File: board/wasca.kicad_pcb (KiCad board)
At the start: 2 copper layers, 100.1 x 77.4 mm, 67 parts, among them CN1 CARTRIDGE_EDGE_CONNECTOR, CN2 TFP09-2-12B, CN3 Conn_02x02_Odd_Even, CN4 SODIMM-200, CN5 693063020911, U1 74ALVC164245, U10 SN74LVC1T45DBV, U11 SN74LVC1T45DBV, U12 SN74LVC1T45DBV, U13 ESP32_CAM_HALF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

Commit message: Cleanup
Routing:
- net /SDRAM_AUX_A2: track 24.3 -> 19.2 mm
- net /SDRAM_AUX_A1: track 20.6 -> 17.4 mm
- net /SDRAM_AUX_A10: track 17.7 -> 15.8 mm
- net /SDRAM_AUX_DQ5: track 26.4 -> 25.4 mm
- net GND: vias 175 -> 176

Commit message: Further cleanup
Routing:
- net /+3_3V: track 379.4 -> 378.7 mm
- net /SDRAM_AUX_DQ7: track 22.3 -> 23.0 mm
- net /SDRAM_AUX_A2: track 19.2 -> 18.7 mm
- net GND: vias 176 -> 180
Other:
- rule pad_to_mask_clearance: 0.05 -> 0

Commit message: Further cleanup
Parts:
- removed TP1, TP2: TestPoint, wasca:TEST_PAD
- added CN6: Conn_01x02_Pin, Connector_PinHeader_2.54mm:PinHeader_1x02_P2.54mm_Vertical, F.Cu at (30.3, 131.4)
- CHAMFER_WARN1, CHAMFER_WARN2: value LOGO -> CHAMFER_WARNING
- moved KICAD1 41.6 mm to (57.6, 96.3)
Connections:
- CN4 pad 150: Net-(CN4-Pad150) -> /TEST_2
- CN4 pad 89: Net-(CN4-Pad89) -> /TEST_1
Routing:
- net /TEST_1: track 0.00 -> 49.3 mm, vias 0 -> 1
- net /TEST_2: track 0.00 -> 30.1 mm, vias 0 -> 1
- net Net-(CN4-Pad150): track 12.0 -> 0.00 mm, vias 1 -> 0
- net Net-(CN4-Pad89): track 2.94 -> 0.00 mm, vias 1 -> 0
- net GND: vias 180 -> 181

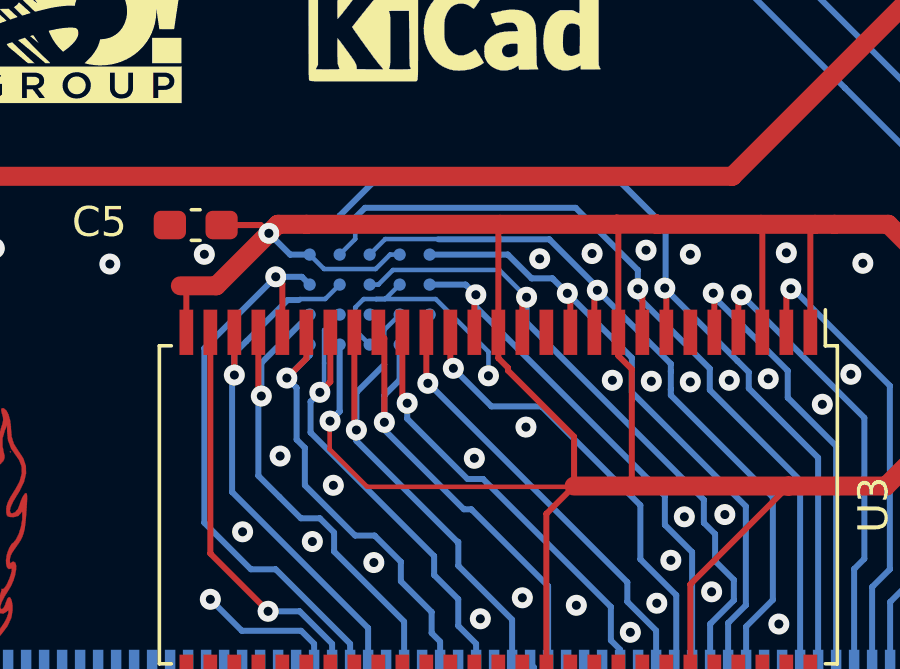
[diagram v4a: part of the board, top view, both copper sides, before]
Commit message: Remove HyperRAM
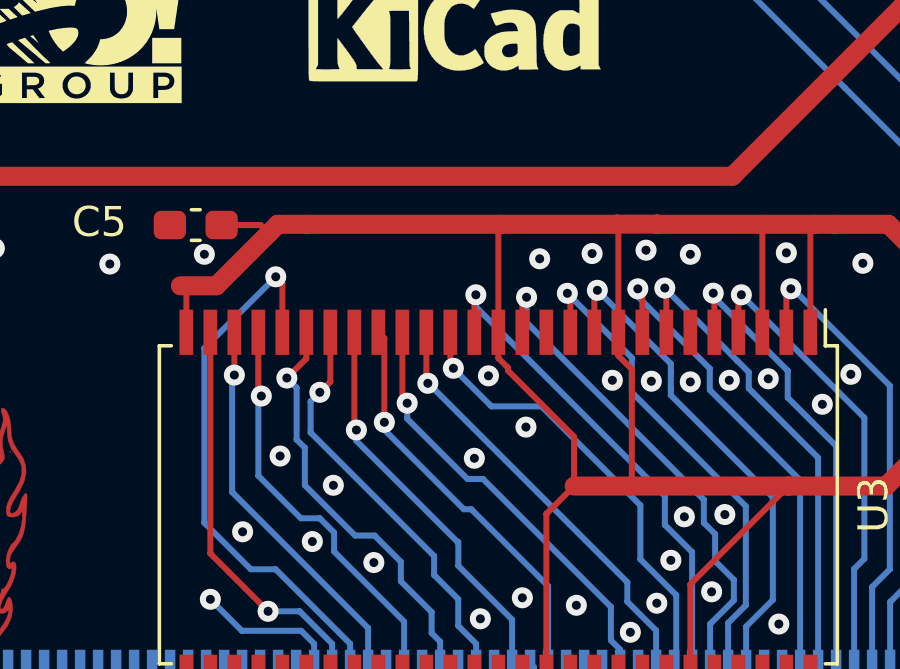
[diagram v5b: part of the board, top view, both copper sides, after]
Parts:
- removed U6: IS66WVH8M8ALL-166B1LI, wasca:BGA25C100P5X5_800X600X120N
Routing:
- net /+3_3V: track 378.7 -> 361.4 mm, vias 22 -> 20
- net /SDRAM_AUX_DQ3: track 30.9 -> 16.7 mm
- net /SDRAM_AUX_DQ4: track 29.8 -> 16.8 mm
- net /SDRAM_AUX_DQ5: track 25.8 -> 17.2 mm
- net GND: track 1221.9 -> 1213.4 mm
- net /SDRAM_AUX_DQ7: track 23.0 -> 17.2 mm
- net /SDRAM_AUX_A2: track 18.7 -> 13.5 mm
- net /SDRAM_AUX_DQ6: track 22.1 -> 16.9 mm
- net /SDRAM_AUX_BA0: track 18.2 -> 13.8 mm
- net /SDRAM_AUX_A1: track 17.4 -> 14.0 mm
- net /SDRAM_AUX_BA1: track 17.0 -> 14.1 mm
- net /SDRAM_AUX_CS: track 16.9 -> 14.1 mm
- net /SDRAM_AUX_DQM0: track 18.8 -> 17.1 mm
- net /SDRAM_AUX_A10: track 15.8 -> 14.3 mm
- net /SDRAM_AUX_A0: track 20.1 -> 18.9 mm

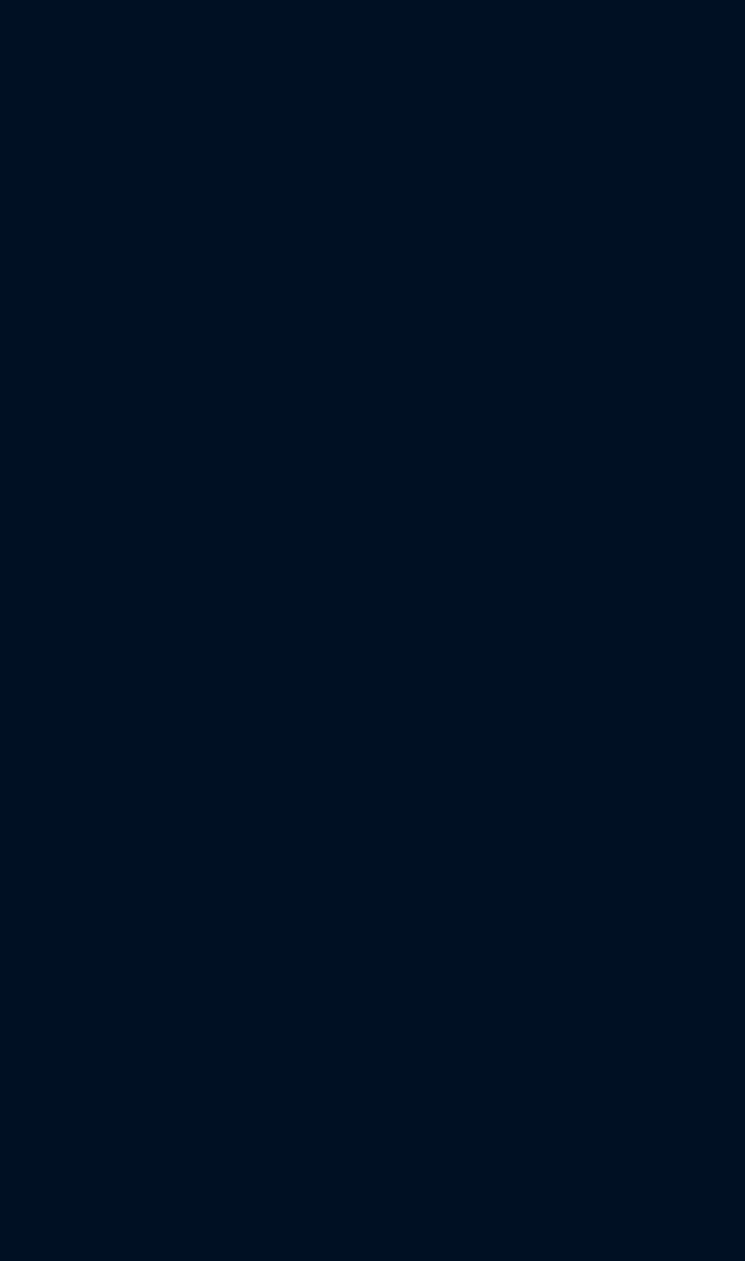
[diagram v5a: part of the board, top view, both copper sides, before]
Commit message: Adding FPGA+power supplies
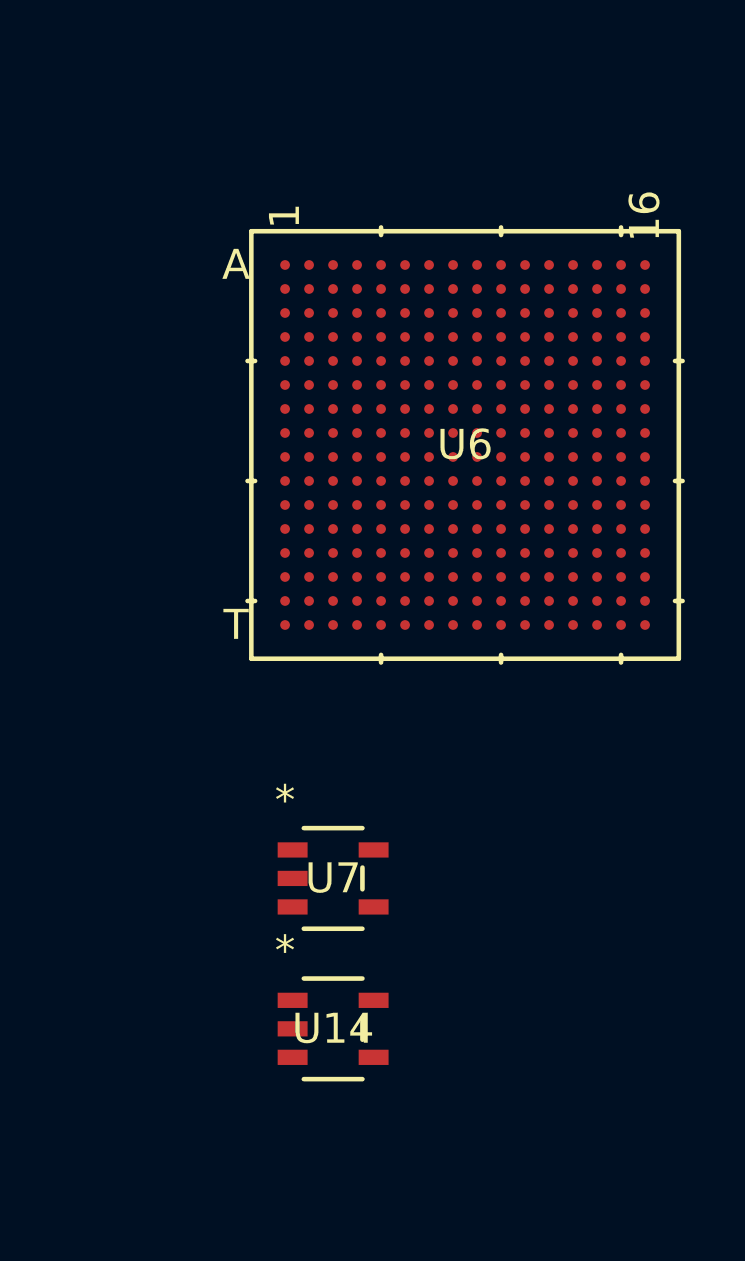
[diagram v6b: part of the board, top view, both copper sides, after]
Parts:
- added U14: SY8008CAAC, wasca:SOT23-5_SY8008B_SGY, F.Cu at (140.4, 115.3)
- added U6: LFE5U-25F-6BG256I, wasca:caBGA256_LAT, F.Cu at (144.8, 95.8)
- added U7: SY8008CAAC, wasca:SOT23-5_SY8008B_SGY, F.Cu at (140.4, 110.3)
